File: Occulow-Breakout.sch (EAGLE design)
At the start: 24 parts

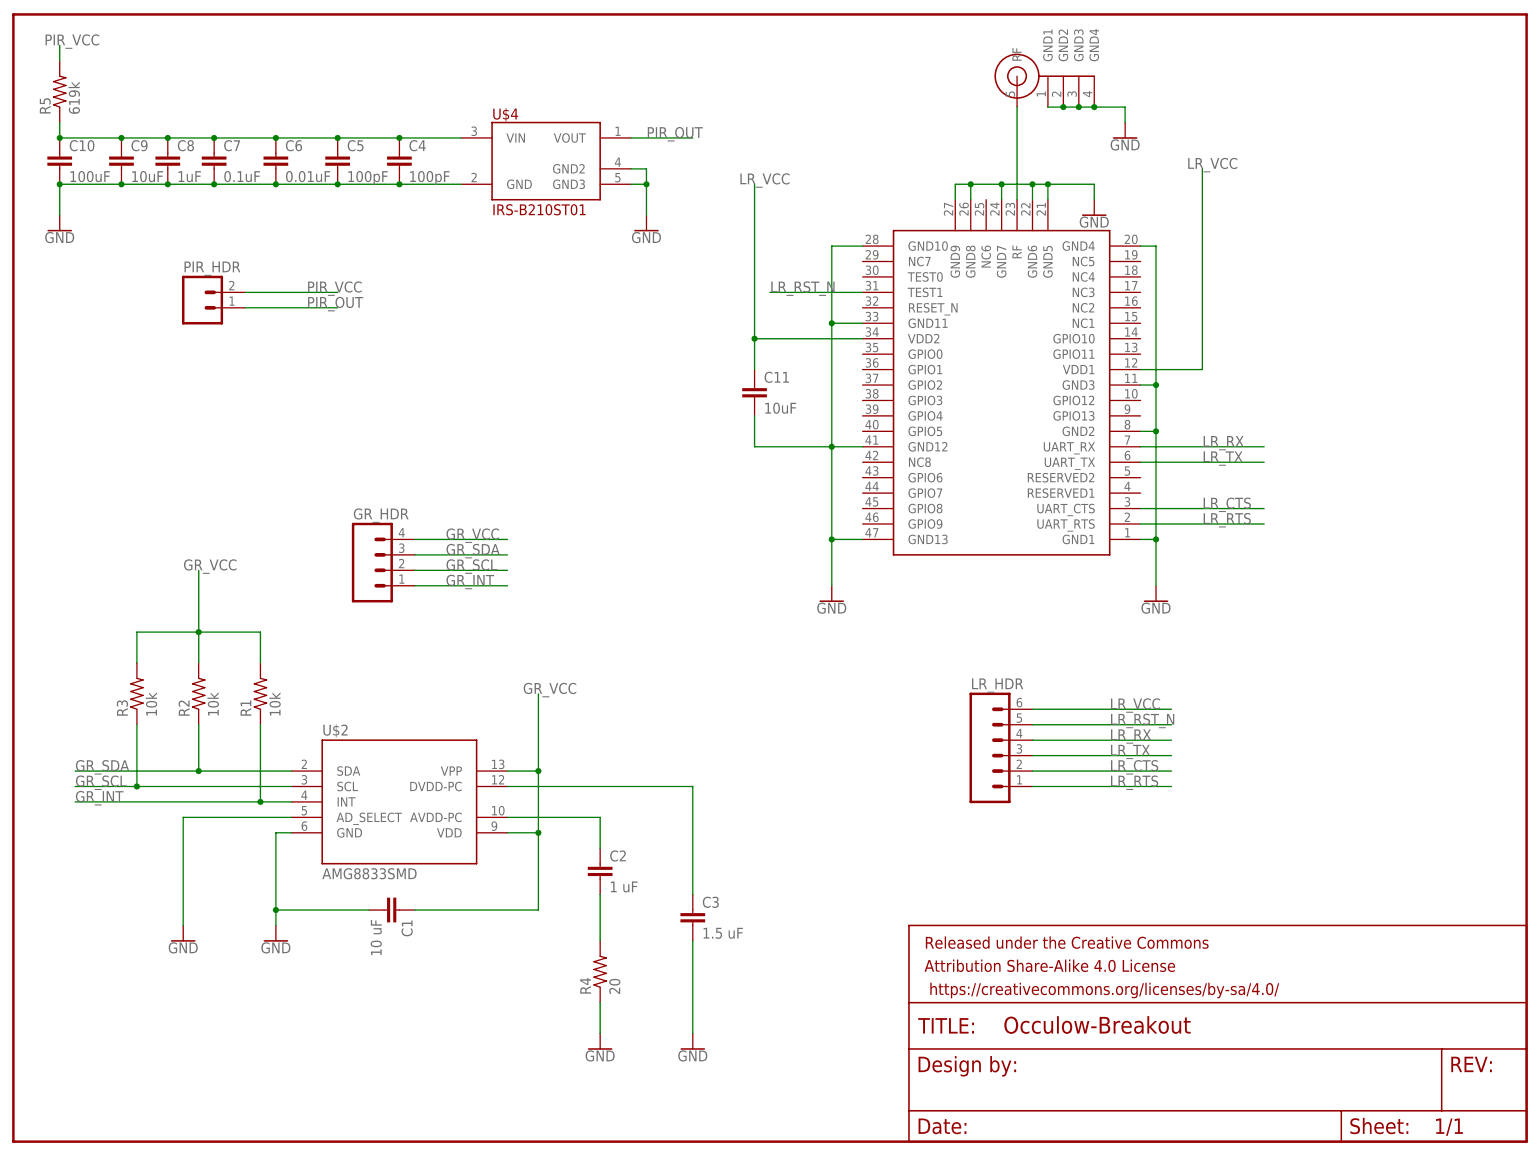
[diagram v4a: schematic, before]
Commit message: Removed excessive caps, first pass at layout on 2x2
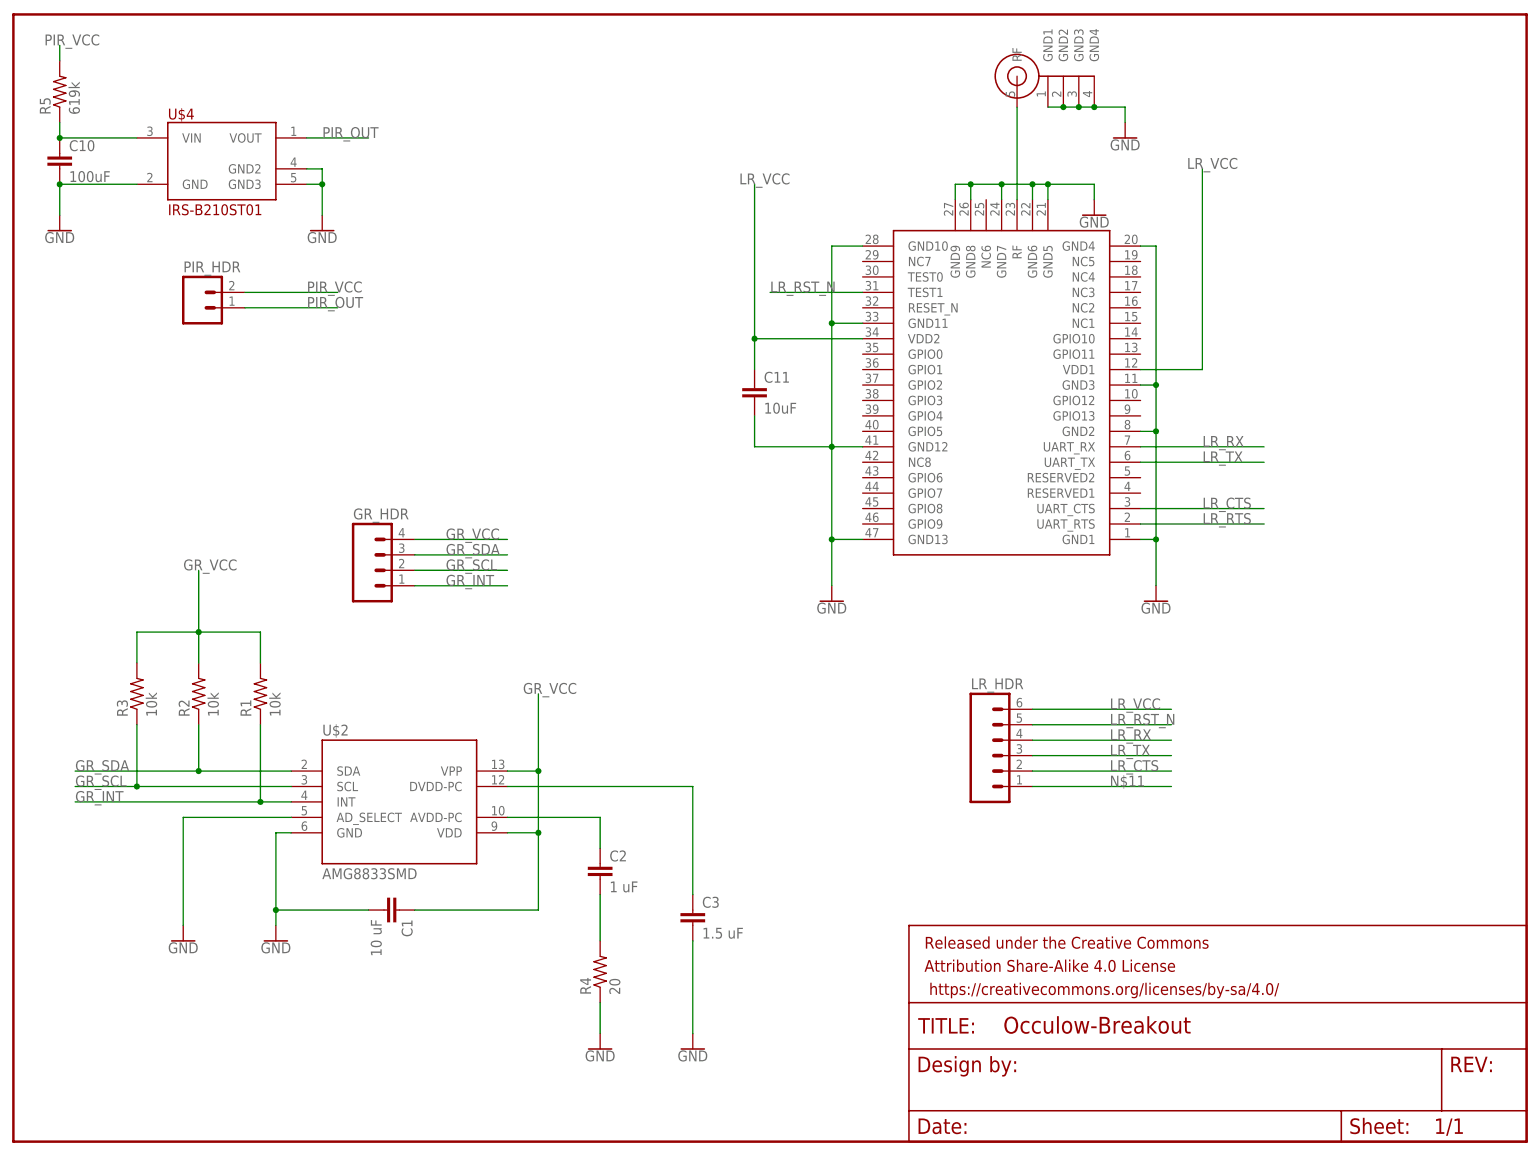
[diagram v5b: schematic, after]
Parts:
- removed C4, C5: 100pF, rcl:C-EUC1206
- removed C6: 0.01uF, rcl:C-EUC1206
- removed C7: 0.1uF, rcl:C-EUC1206
- removed C8: 1uF, rcl:C-EUC1206
- removed C9: 10uF, rcl:C-EUC1206
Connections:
- new net N$11: LR_HDR.1
- net GND: no longer C4.2, C5.2, C6.2, C7.2, C8.2, C9.2
- net LR_RTS: no longer LR_HDR.1
- net N$5: no longer C4.1, C5.1, C6.1, C7.1, C8.1, C9.1
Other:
- moved on the sheet: U$4
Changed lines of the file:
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@@
 <part name="U$4" library="PIR" deviceset="IRS-B210ST01" device=""/>
 <part name="GND9" library="SparkFun-PowerSymbols" deviceset="GND" device=""/>
-<part name="C4" library="rcl" deviceset="C-EU" device="C1206" value="100pF"/>
-<part name="C5" library="rcl" deviceset="C-EU" device="C1206" value="100pF"/>
-<part name="C6" library="rcl" deviceset="C-EU" device="C1206" value="0.01uF"/>
-<part name="C7" library="rcl" deviceset="C-EU" device="C1206" value="0.1uF"/>
-<part name="C8" library="rcl" deviceset="C-EU" device="C1206" value="1uF"/>
-<part name="C9" library="rcl" deviceset="C-EU" device="C1206" value="10uF"/>
 <part name="C10" library="rcl" deviceset="C-EU" device="C1206" value="100uF"/>
 <part name="GND10" library="SparkFun-PowerSymbols" deviceset="GND" device=""/>
@@
 <instance part="GND7" gate="1" x="350.52" y="83.82"/>
 <instance part="GND8" gate="1" x="297.18" y="83.82"/>
-<instance part="U$4" gate="G$1" x="246.38" y="157.48"/>
-<instance part="GND9" gate="1" x="266.7" y="144.78"/>
-<instance part="C4" gate="G$1" x="226.06" y="157.48"/>
-<instance part="C5" gate="G$1" x="215.9" y="157.48"/>
-<instance part="C6" gate="G$1" x="205.74" y="157.48"/>
-<instance part="C7" gate="G$1" x="195.58" y="157.48"/>
-<instance part="C8" gate="G$1" x="187.96" y="157.48"/>
-<instance part="C9" gate="G$1" x="180.34" y="157.48"/>
+<instance part="U$4" gate="G$1" x="193.04" y="157.48"/>
+<instance part="GND9" gate="1" x="213.36" y="144.78"/>
 <instance part="C10" gate="G$1" x="170.18" y="157.48"/>
 <instance part="GND10" gate="1" x="170.18" y="144.78"/>
@@
 <pinref part="U$4" gate="G$1" pin="GND2"/>
 <pinref part="GND9" gate="1" pin="GND"/>
-<wire x1="264.16" y1="154.94" x2="266.7" y2="154.94" width="0.1524" layer="91"/>
-<wire x1="266.7" y1="154.94" x2="266.7" y2="152.4" width="0.1524" layer="91"/>
+<wire x1="210.82" y1="154.94" x2="213.36" y2="154.94" width="0.1524" layer="91"/>
+<wire x1="213.36" y1="154.94" x2="213.36" y2="152.4" width="0.1524" layer="91"/>
 <pinref part="U$4" gate="G$1" pin="GND3"/>
-<wire x1="266.7" y1="152.4" x2="266.7" y2="147.32" width="0.1524" layer="91"/>
-<wire x1="264.16" y1="152.4" x2="266.7" y2="152.4" width="0.1524" layer="91"/>
-<junction x="266.7" y="152.4"/>
+<wire x1="213.36" y1="152.4" x2="213.36" y2="147.32" width="0.1524" layer="91"/>
+<wire x1="210.82" y1="152.4" x2="213.36" y2="152.4" width="0.1524" layer="91"/>
+<junction x="213.36" y="152.4"/>
 </segment>
 <segment>
 <pinref part="U$4" gate="G$1" pin="GND"/>
-<pinref part="C4" gate="G$1" pin="2"/>
-<wire x1="236.22" y1="152.4" x2="226.06" y2="152.4" width="0.1524" layer="91"/>
-<pinref part="C5" gate="G$1" pin="2"/>
-<wire x1="226.06" y1="152.4" x2="215.9" y2="152.4" width="0.1524" layer="91"/>
-<junction x="226.06" y="152.4"/>
-<pinref part="C6" gate="G$1" pin="2"/>
-<wire x1="215.9" y1="152.4" x2="205.74" y2="152.4" width="0.1524" layer="91"/>
-<junction x="215.9" y="152.4"/>
-<pinref part="C7" gate="G$1" pin="2"/>
-<wire x1="205.74" y1="152.4" x2="195.58" y2="152.4" width="0.1524" layer="91"/>
-<junction x="205.74" y="152.4"/>
-<pinref part="C8" gate="G$1" pin="2"/>
-<wire x1="195.58" y1="152.4" x2="187.96" y2="152.4" width="0.1524" layer="91"/>
-<junction x="195.58" y="152.4"/>
-<pinref part="C9" gate="G$1" pin="2"/>
-<wire x1="187.96" y1="152.4" x2="180.34" y2="152.4" width="0.1524" layer="91"/>
-<junction x="187.96" y="152.4"/>
+<wire x1="182.88" y1="152.4" x2="170.18" y2="152.4" width="0.1524" layer="91"/>
 <pinref part="C10" gate="G$1" pin="2"/>
-<wire x1="180.34" y1="152.4" x2="170.18" y2="152.4" width="0.1524" layer="91"/>
-<junction x="180.34" y="152.4"/>
 <pinref part="GND10" gate="1" pin="GND"/>
 <wire x1="170.18" y1="152.4" x2="170.18" y2="147.32" width="0.1524" layer="91"/>
@@
 <label x="358.14" y="96.52" size="1.778" layer="95"/>
 </segment>
-<segment>
-<pinref part="LR_HDR" gate="G$1" pin="1"/>
-<wire x1="330.2" y1="53.34" x2="353.06" y2="53.34" width="0.1524" layer="91"/>
-<label x="342.9" y="53.34" size="1.778" layer="95"/>
-</segment>
 </net>
 <net name="N$5" class="0">
 <segment>
 <pinref part="U$4" gate="G$1" pin="VIN"/>
-<pinref part="C4" gate="G$1" pin="1"/>
-<wire x1="236.22" y1="160.02" x2="226.06" y2="160.02" width="0.1524" layer="91"/>
-<pinref part="C5" gate="G$1" pin="1"/>
-<wire x1="226.06" y1="160.02" x2="215.9" y2="160.02" width="0.1524" layer="91"/>
-<junction x="226.06" y="160.02"/>
-<pinref part="C6" gate="G$1" pin="1"/>
-<wire x1="215.9" y1="160.02" x2="205.74" y2="160.02" width="0.1524" layer="91"/>
-<junction x="215.9" y="160.02"/>
-<pinref part="C7" gate="G$1" pin="1"/>
-<wire x1="205.74" y1="160.02" x2="195.58" y2="160.02" width="0.1524" layer="91"/>
-<junction x="205.74" y="160.02"/>
-<pinref part="C8" gate="G$1" pin="1"/>
-<wire x1="195.58" y1="160.02" x2="187.96" y2="160.02" width="0.1524" layer="91"/>
-<junction x="195.58" y="160.02"/>
-<pinref part="C9" gate="G$1" pin="1"/>
-<wire x1="187.96" y1="160.02" x2="180.34" y2="160.02" width="0.1524" layer="91"/>
-<junction x="187.96" y="160.02"/>
+<wire x1="182.88" y1="160.02" x2="170.18" y2="160.02" width="0.1524" layer="91"/>
 <pinref part="C10" gate="G$1" pin="1"/>
-<wire x1="180.34" y1="160.02" x2="170.18" y2="160.02" width="0.1524" layer="91"/>
-<junction x="180.34" y="160.02"/>
 <pinref part="R5" gate="G$1" pin="1"/>
 <wire x1="170.18" y1="160.02" x2="170.18" y2="162.56" width="0.1524" layer="91"/>
@@
 <segment>
 <pinref part="U$4" gate="G$1" pin="VOUT"/>
-<wire x1="264.16" y1="160.02" x2="274.32" y2="160.02" width="0.1524" layer="91"/>
-<label x="266.7" y="160.02" size="1.778" layer="95"/>
+<wire x1="210.82" y1="160.02" x2="220.98" y2="160.02" width="0.1524" layer="91"/>
+<label x="213.36" y="160.02" size="1.778" layer="95"/>
 </segment>
 <segment>
@@
 </segment>
 </net>
+<net name="N$11" class="0">
+<segment>
+<pinref part="LR_HDR" gate="G$1" pin="1"/>
+<wire x1="330.2" y1="53.34" x2="353.06" y2="53.34" width="0.1524" layer="91"/>
+<label x="342.9" y="53.34" size="1.778" layer="95"/>
+</segment>
+</net>
